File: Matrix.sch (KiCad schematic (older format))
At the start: 115 parts

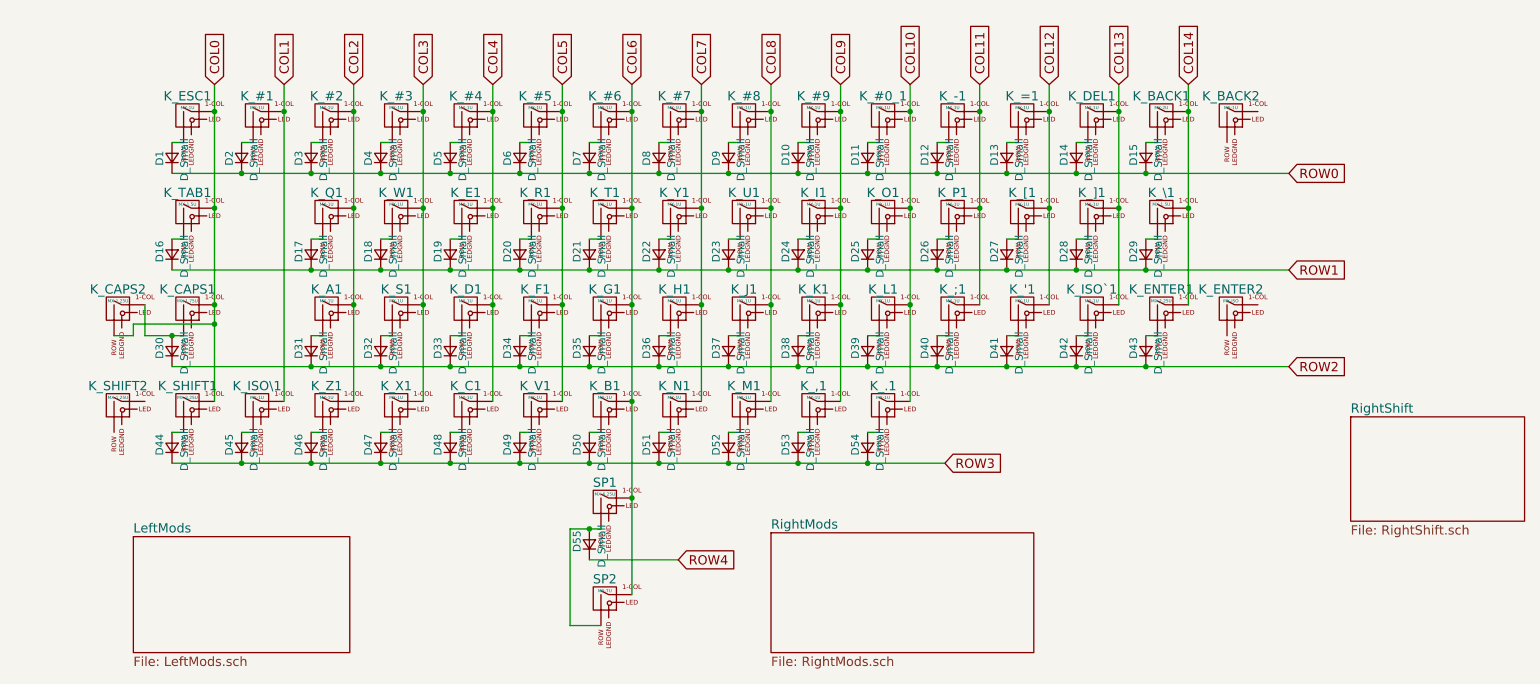
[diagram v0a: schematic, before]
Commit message: Wire more compat footprints
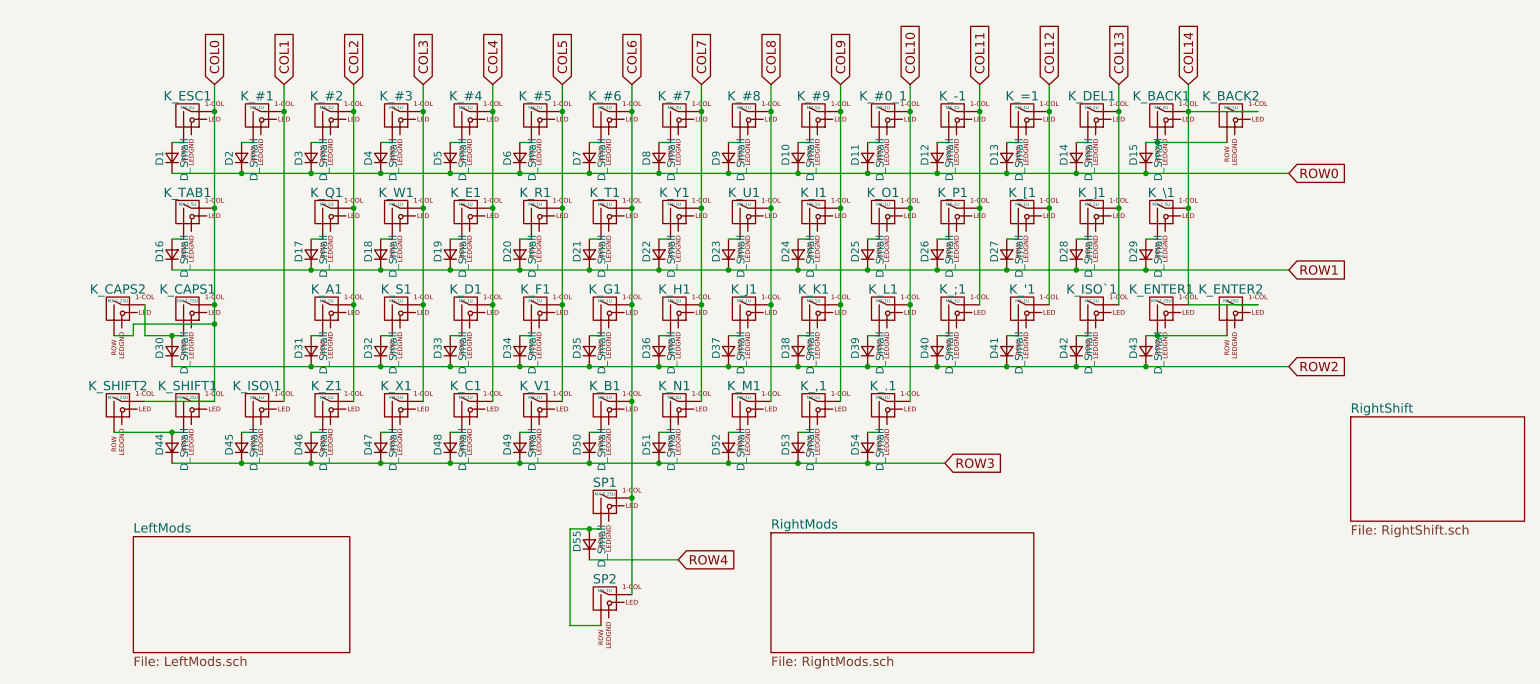
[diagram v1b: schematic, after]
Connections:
- net COL0: now also K_SHIFT2.1 (COL)
- net COL14: now also K_BACK2.1 (COL), K_ENTER2.1 (COL)
- net at D15.2 (A), K_BACK1.2 (ROW): now also K_BACK2.2 (ROW)
- net at D43.2 (A), K_ENTER1.2 (ROW): now also K_ENTER2.2 (ROW)
- net at D44.2 (A), K_SHIFT1.2 (ROW): now also K_SHIFT2.2 (ROW)
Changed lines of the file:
@@
 $EndComp
 Wire Wire Line
-	7775 1400 7700 1400
+	7700 1400 8225 1400
 $Comp
 L MX-1U K_TAB1
@@
 $EndComp
 Wire Wire Line
-	7775 2650 7700 2650
+	7700 2650 8225 2650
 $Comp
 L MX-1U K_SHIFT1
@@
 $EndComp
 Wire Wire Line
-	1475 3275 1400 3275
+	1025 3275 1475 3275
 $Comp
 L MX-1U K_ISO\1
@@
 	3975 3900 3975 4525
 Connection ~ 4100 3900
+Wire Wire Line
+	7975 2450 8425 2450
+Connection ~ 7775 2650
+Wire Wire Line
+	7975 1200 8425 1200
+Connection ~ 7775 1400
+Wire Wire Line
+	1675 3075 1225 3075
+Connection ~ 1400 3275
 $EndSCHEMATC

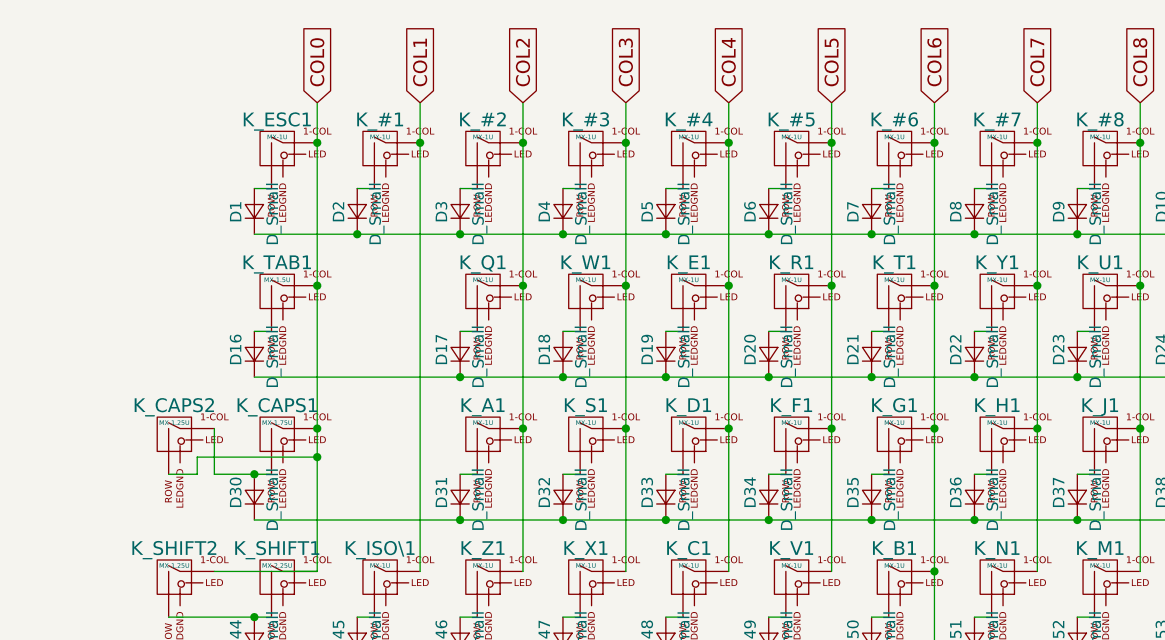
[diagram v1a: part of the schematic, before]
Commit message: Begin routing LED rows
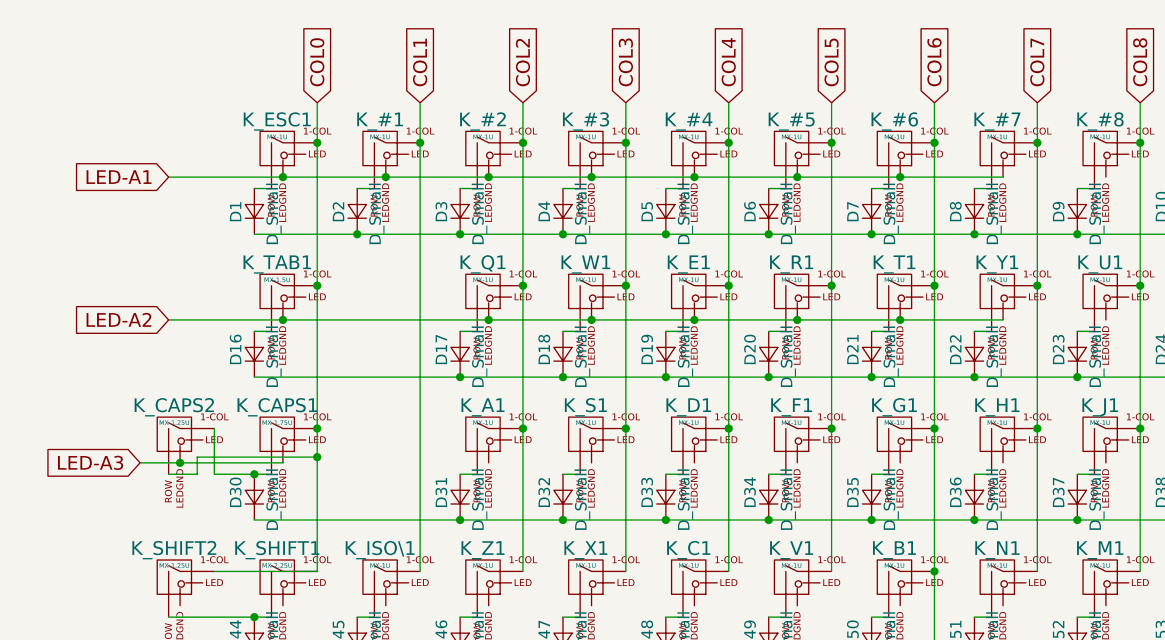
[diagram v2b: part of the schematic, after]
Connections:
- net LED-A1: now reaches K_ESC1.4 (LEDGND)
- net LED-A1: now also K_#1.4 (LEDGND), K_#2.4 (LEDGND), K_#3.4 (LEDGND), K_#4.4 (LEDGND), K_#5.4 (LEDGND), K_#6.4 (LEDGND), K_#7.4 (LEDGND)
- net LED-A2: now reaches K_TAB1.4 (LEDGND)
- net LED-A2: now also K_E1.4 (LEDGND), K_Q1.4 (LEDGND), K_R1.4 (LEDGND), K_T1.4 (LEDGND), K_W1.4 (LEDGND), K_Y1.4 (LEDGND)
- net LED-A3: now reaches K_CAPS1.4 (LEDGND)
- net LED-A3: now also K_CAPS2.4 (LEDGND)

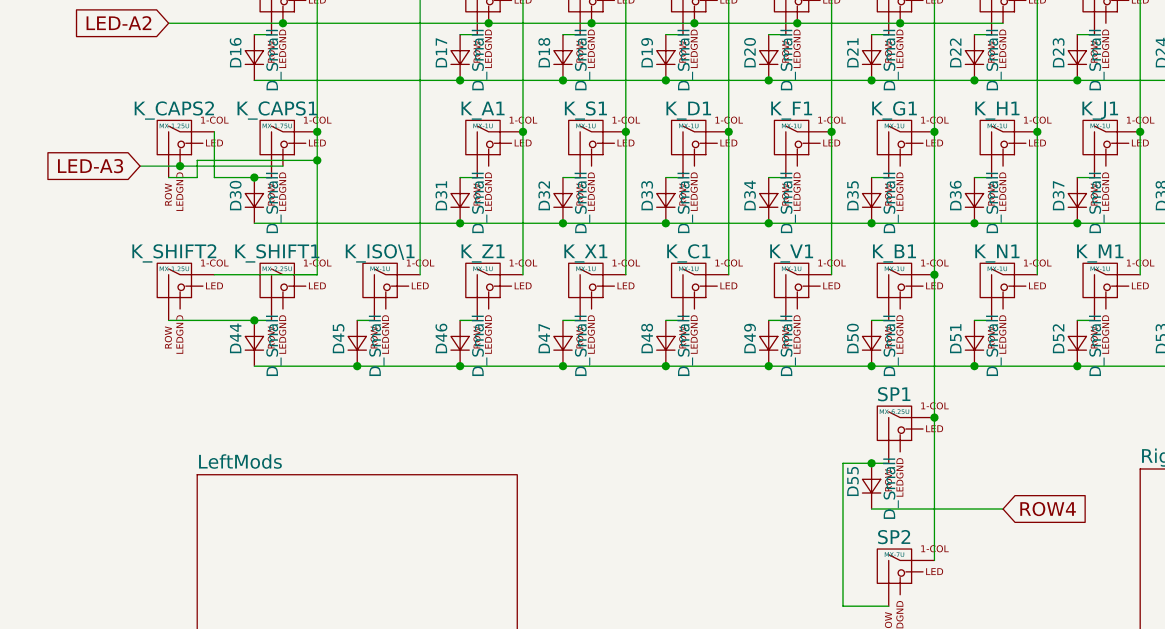
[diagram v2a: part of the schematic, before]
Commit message: Route left half LED rows
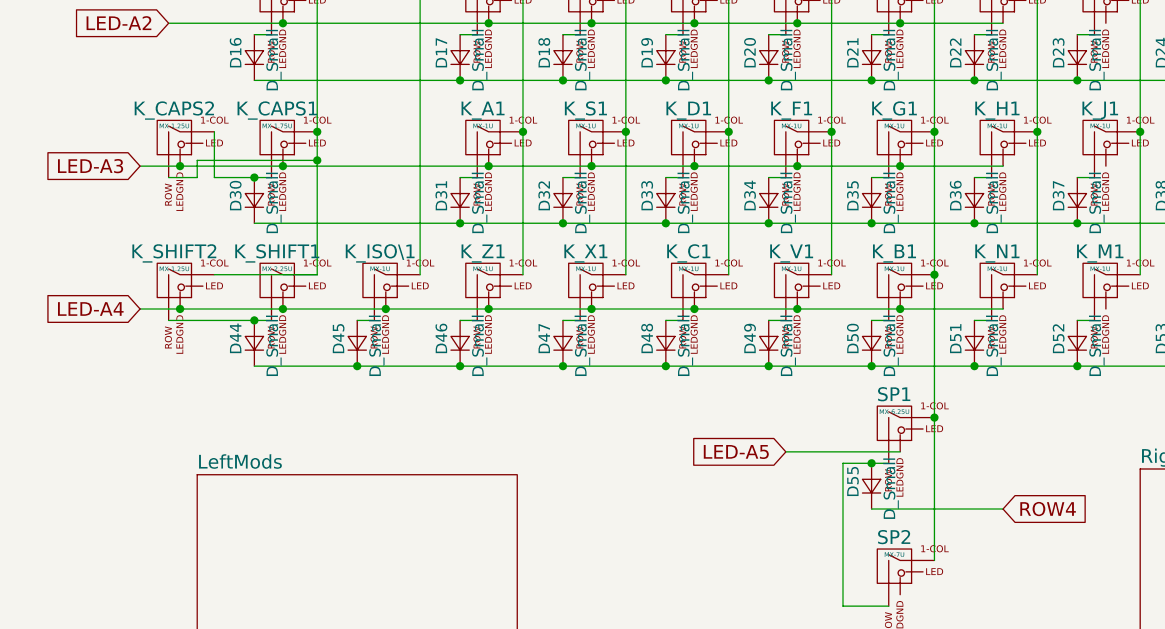
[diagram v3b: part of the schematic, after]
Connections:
- net LED-A3: now also K_A1.4 (LEDGND), K_D1.4 (LEDGND), K_F1.4 (LEDGND), K_G1.4 (LEDGND), K_H1.4 (LEDGND), K_S1.4 (LEDGND)
- net LED-A4: now reaches K_SHIFT1.4 (LEDGND)
- net LED-A4: now also K_B1.4 (LEDGND), K_C1.4 (LEDGND), K_ISO\1.4 (LEDGND), K_N1.4 (LEDGND), K_SHIFT2.4 (LEDGND), K_V1.4 (LEDGND), K_X1.4 (LEDGND), K_Z1.4 (LEDGND)
- net LED-A5: now reaches SP1.4 (LEDGND)
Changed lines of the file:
@@
 Text GLabel 1025 1350 0    60   Input ~ 0
 LED-A1
+Text GLabel 1025 1975 0    60   Input ~ 0
+LED-A2
+Text GLabel 900  2600 0    60   Input ~ 0
+LED-A3
 Wire Wire Line
 	1475 1400 1400 1400
@@
 Wire Wire Line
 	1025 1975 4675 1975
-Text GLabel 1025 1975 0    60   Input ~ 0
-LED-A2
 Connection ~ 1525 1975
 Connection ~ 2425 1975
@@
 Connection ~ 4225 1975
 Wire Wire Line
-	900  2600 1525 2600
+	900  2600 4675 2600
 Connection ~ 1075 2600
-Text GLabel 900  2600 0    60   Input ~ 0
-LED-A3
+Connection ~ 1525 2600
+Connection ~ 2425 2600
+Connection ~ 2875 2600
+Connection ~ 3325 2600
+Connection ~ 3775 2600
+Connection ~ 4225 2600
+Wire Wire Line
+	900  3225 4675 3225
+Connection ~ 1075 3225
+Text GLabel 900  3225 0    60   Input ~ 0
+LED-A4
+Connection ~ 1525 3225
+Connection ~ 1975 3225
+Connection ~ 2875 3225
+Connection ~ 2425 3225
+Connection ~ 3325 3225
+Connection ~ 3775 3225
+Connection ~ 4225 3225
+Wire Wire Line
+	4225 3850 3725 3850
+Text GLabel 3725 3850 0    60   Input ~ 0
+LED-A5
 $EndSCHEMATC

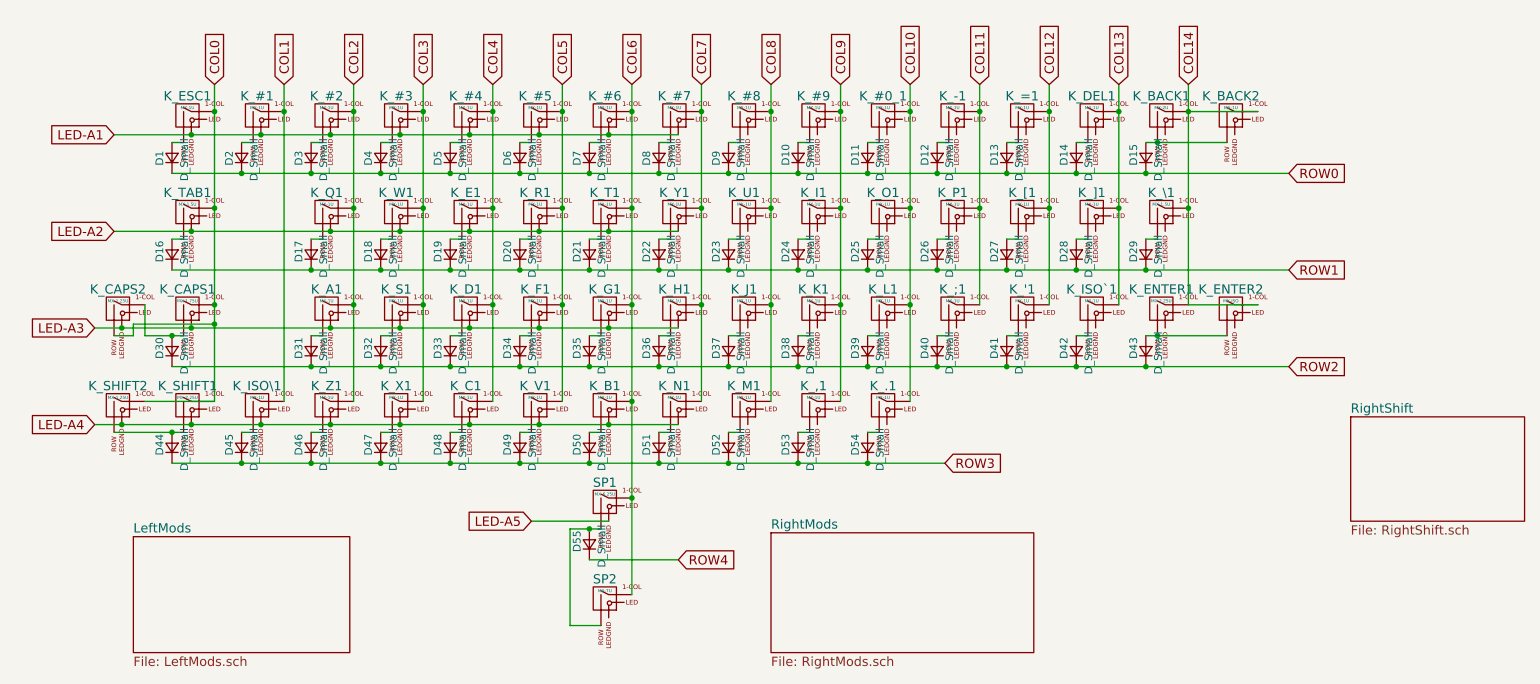
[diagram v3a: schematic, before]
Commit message: Unroute LEDs
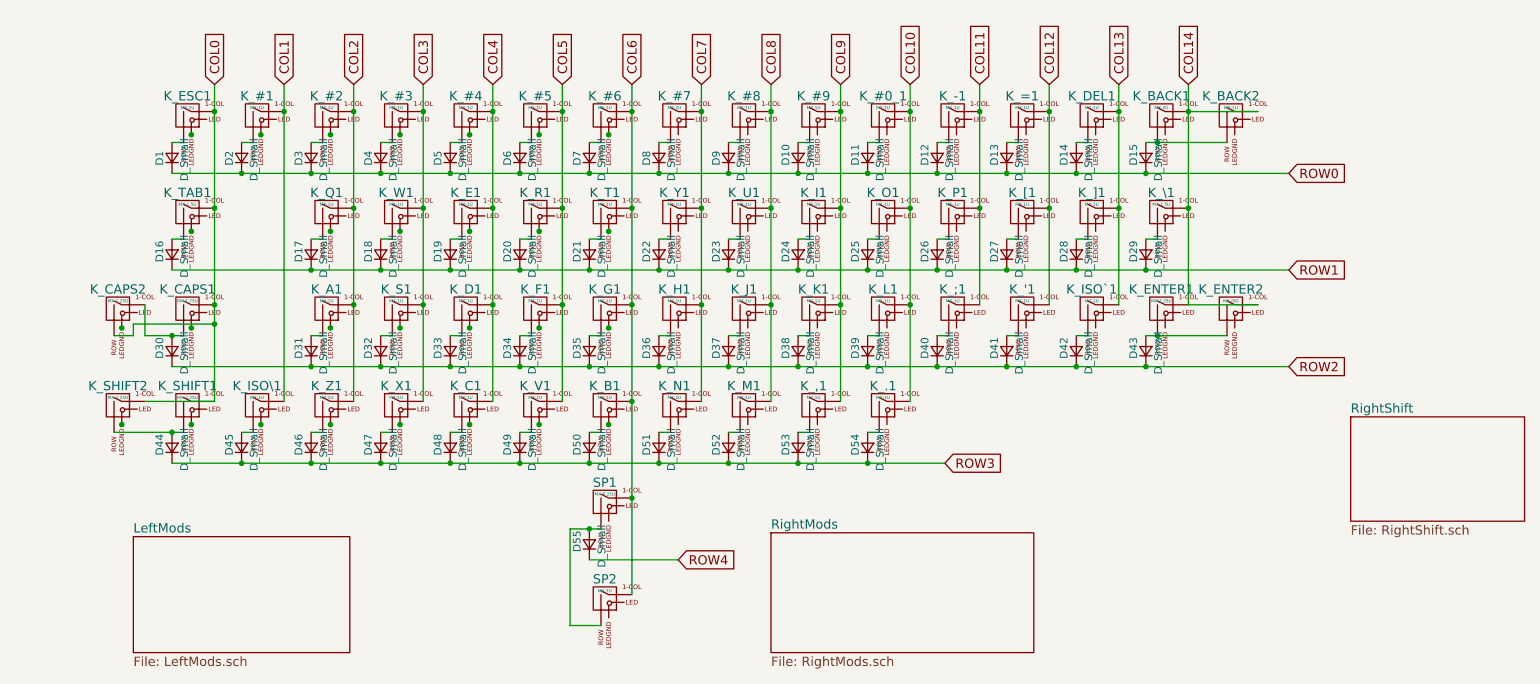
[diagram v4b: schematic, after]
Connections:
- removed net LED-A1: K_#1.4 (LEDGND), K_#2.4 (LEDGND), K_#3.4 (LEDGND), K_#4.4 (LEDGND), K_#5.4 (LEDGND), K_#6.4 (LEDGND), K_#7.4 (LEDGND), K_ESC1.4 (LEDGND)
- removed net LED-A2: K_E1.4 (LEDGND), K_Q1.4 (LEDGND), K_R1.4 (LEDGND), K_T1.4 (LEDGND), K_TAB1.4 (LEDGND), K_W1.4 (LEDGND), K_Y1.4 (LEDGND)
- removed net LED-A3: K_A1.4 (LEDGND), K_CAPS1.4 (LEDGND), K_CAPS2.4 (LEDGND), K_D1.4 (LEDGND), K_F1.4 (LEDGND), K_G1.4 (LEDGND), K_H1.4 (LEDGND), K_S1.4 (LEDGND)
- removed net LED-A4: K_B1.4 (LEDGND), K_C1.4 (LEDGND), K_ISO\1.4 (LEDGND), K_N1.4 (LEDGND), K_SHIFT1.4 (LEDGND), K_SHIFT2.4 (LEDGND), K_V1.4 (LEDGND), K_X1.4 (LEDGND), K_Z1.4 (LEDGND)
- net LED-A5: no longer names the net of SP1.4 (LEDGND)
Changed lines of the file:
@@
 Text GLabel 4675 4100 2    60   Input ~ 0
 ROW4
-Text GLabel 1025 1350 0    60   Input ~ 0
-LED-A1
-Text GLabel 1025 1975 0    60   Input ~ 0
-LED-A2
-Text GLabel 900  2600 0    60   Input ~ 0
-LED-A3
 Wire Wire Line
 	1475 1400 1400 1400
@@
 	1675 3075 1225 3075
 Connection ~ 1400 3275
-Wire Wire Line
-	1025 1350 4675 1350
 Connection ~ 1525 1350
 Connection ~ 1975 1350
@@
 Connection ~ 3775 1350
 Connection ~ 4225 1350
-Wire Wire Line
-	1025 1975 4675 1975
 Connection ~ 1525 1975
 Connection ~ 2425 1975
@@
 Connection ~ 3775 1975
 Connection ~ 4225 1975
-Wire Wire Line
-	900  2600 4675 2600
 Connection ~ 1075 2600
 Connection ~ 1525 2600
@@
 Connection ~ 3775 2600
 Connection ~ 4225 2600
-Wire Wire Line
-	900  3225 4675 3225
 Connection ~ 1075 3225
-Text GLabel 900  3225 0    60   Input ~ 0
-LED-A4
 Connection ~ 1525 3225
 Connection ~ 1975 3225
@@
 Connection ~ 3775 3225
 Connection ~ 4225 3225
-Wire Wire Line
-	4225 3850 3725 3850
-Text GLabel 3725 3850 0    60   Input ~ 0
-LED-A5
 $EndSCHEMATC

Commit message: Swap footprints for No-LED counterparts
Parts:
- K_#0_1, K_#1, K_#2, K_#3, K_#4, K_#5, K_#6, K_#7, K_#8, K_#9, K_'1, K_,1, K_-1, K_.1, K_;1, K_=1, K_A1, K_B1, K_BACK2, K_C1, K_D1, K_DEL1, K_E1, K_ESC1, K_F1, K_G1, K_H1, K_I1, K_ISO\1, K_ISO`1, K_J1, K_K1, K_L1, K_M1, K_N1, K_O1, K_P1, K_Q1, K_R1, K_S1, K_T1, K_U1, K_V1, K_W1, K_X1, K_Y1, K_Z1, K_[1, K_]1: footprint MX_Alps_Hybrid:MX-1U -> MX_Alps_Hybrid:MX-1U-NoLED
- K_BACK1: footprint MX_Alps_Hybrid:MX-2U -> MX_Alps_Hybrid:MX-1U-NoLED
- K_CAPS1: footprint MX_Alps_Hybrid:MX-1.75U -> MX_Alps_Hybrid:MX-1.75U-NoLED
- K_CAPS2: footprint MX_Alps_Hybrid:MX-1.25U-FLIPPED -> MX_Alps_Hybrid:MX-1.25U-NoLED
- K_ENTER1, K_SHIFT1: footprint MX_Alps_Hybrid:MX-2.25U -> MX_Alps_Hybrid:MX-2.25U-NoLED
- K_ENTER2: footprint MX_Alps_Hybrid:MX-ISO-Combined-ReversedStabilizers -> MX_Alps_Hybrid:MX-ISO-Combined-ReversedStabilizers-NoLED
- K_SHIFT2: footprint MX_Alps_Hybrid:MX-1.25U -> MX_Alps_Hybrid:MX-1.25U-NoLED
- K_TAB1, K_\1: footprint MX_Alps_Hybrid:MX-1.5U -> MX_Alps_Hybrid:MX-1.5U-NoLED
- SP1: footprint MX_Alps_Hybrid:MX-6.25U-ReversedStabilizers -> MX_Alps_Hybrid:MX-6.25U-ReversedStabilizers-NoLED
- SP2: footprint MX_Alps_Hybrid:MX-7U-ReversedStabilizers -> MX_Alps_Hybrid:MX-7U-ReversedStabilizers-NoLED
